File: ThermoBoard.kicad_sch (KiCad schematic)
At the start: 4 parts

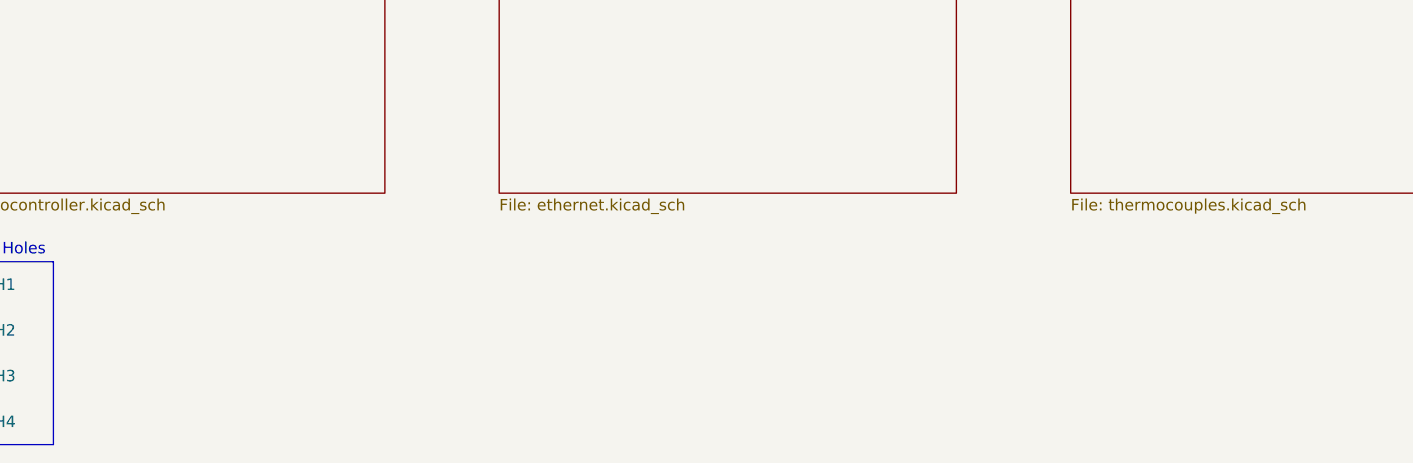
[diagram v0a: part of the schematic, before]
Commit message: Rev 1B - Fix silkscreen, board outline, ethernet pinout
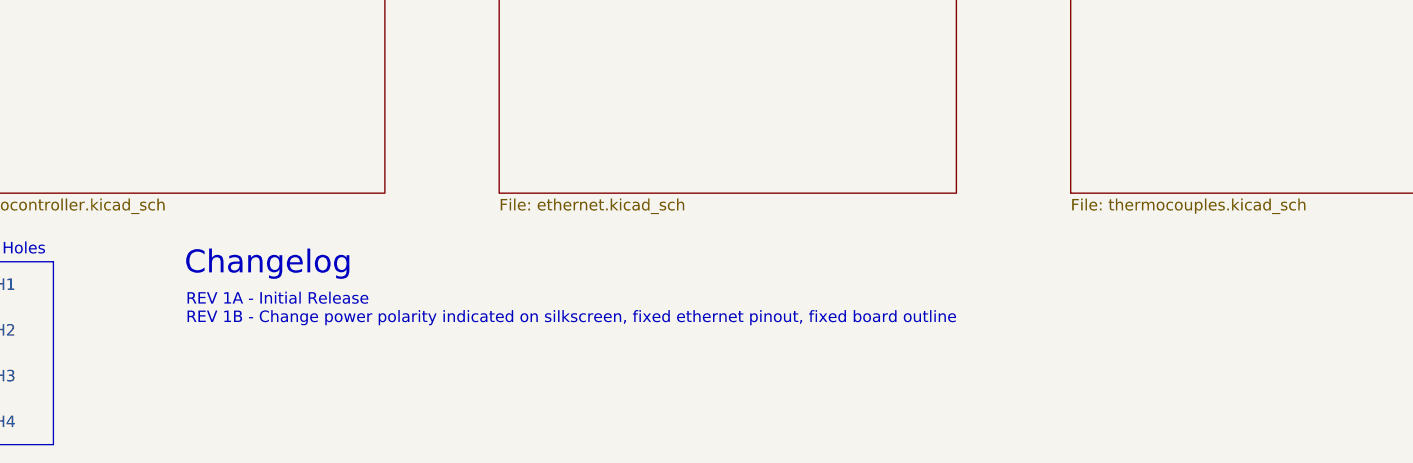
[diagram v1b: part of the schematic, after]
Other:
- note added: "Changelog"
- note added: "REV 1A - Initial Release REV 1B - Change power polarity indicated on silkscreen, fixed ethernet pinout, fixed board outline"
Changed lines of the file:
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@@
 		(title "Thermocouple Board")
 		(date "2025-10-15")
-		(rev "1A")
+		(rev "1B")
 		(company "Aggie Propulsion and Rocketry Lab")
 		(comment 1 "Drawn by: Nolan Poe")
@@
 		)
 	)
+	(text "Changelog"
+		(exclude_from_sim no)
+		(at 56.896 169.164 0)
+		(effects
+			(font
+				(size 2.54 2.54)
+			)
+		)
+	)
 	(text "APRL Thermocouple Board"
 		(exclude_from_sim no)
@@
 		)
 	)
+	(text "REV 1A - Initial Release\nREV 1B - Change power polarity indicated on silkscreen, fixed ethernet pinout, fixed board outline"
+		(exclude_from_sim no)
+		(at 47.752 174.244 0)
+		(effects
+			(font
+				(size 1.27 1.27)
+			)
+			(justify left)
+		)
+	)
